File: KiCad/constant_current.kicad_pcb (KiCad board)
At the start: 2 copper layers, 15.2 x 16.5 mm, 18 parts, among them Q1 BC817-40

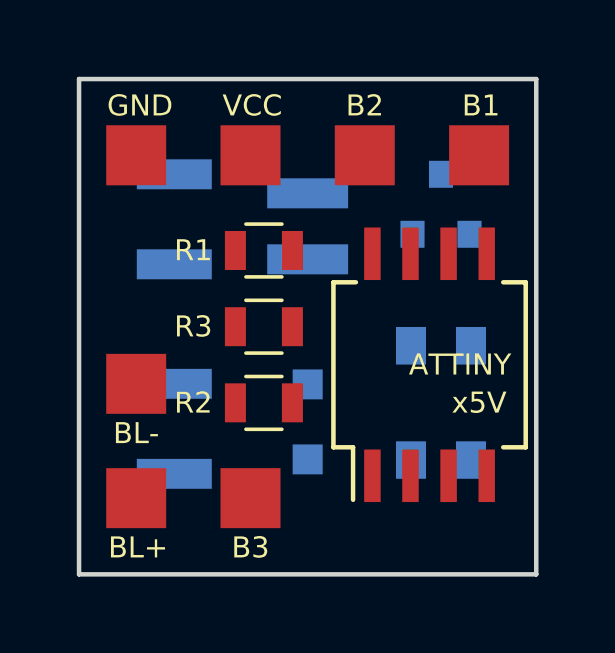
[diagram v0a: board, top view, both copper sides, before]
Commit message: Changed Footprint of Attiny
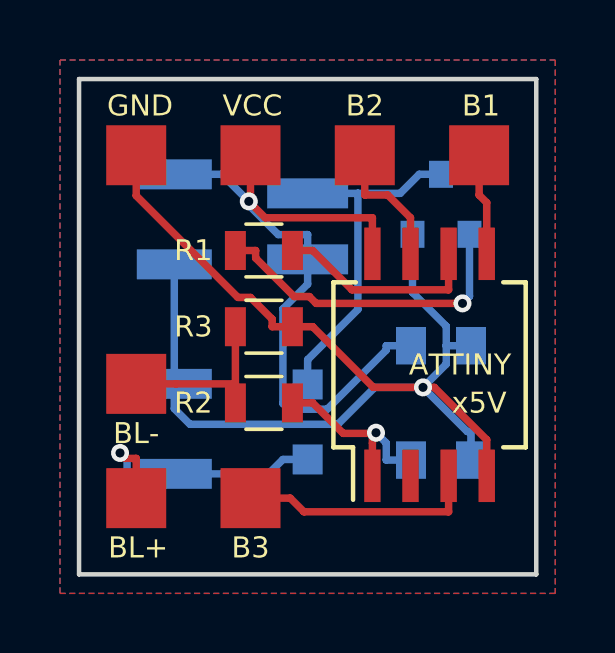
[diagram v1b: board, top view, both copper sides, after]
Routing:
- net GND: track 0.00 -> 41.5 mm, vias 0 -> 1
- net VCC: track 0.00 -> 23.7 mm, vias 0 -> 1
- net Net-(D1-Pad2): track 0.00 -> 11.8 mm
- net Net-(Q1-Pad1): track 0.00 -> 10.8 mm, vias 0 -> 1
- net Net-(C2-Pad1): track 0.00 -> 8.95 mm, vias 0 -> 1
- net Net-(IC1-Pad3): track 0.00 -> 7.99 mm
- net Net-(IC1-Pad6): track 0.00 -> 6.95 mm
- net Net-(C3-Pad2): track 0.00 -> 6.51 mm, vias 0 -> 1
- net Net-(R2-Pad2): track 0.00 -> 5.85 mm
- net Net-(IC1-Pad7): track 0.00 -> 4.36 mm
- net Net-(IC1-Pad5): track 0.00 -> 3.39 mm
- added copper zone on B.Cu, net GND
- added copper zone on F.Cu, net GND
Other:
- rule pad_to_mask_clearance: 0.2 -> 0

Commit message: changed inductor footprint
Changed inductor footprint for easyer handsoldering
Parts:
- L1: footprint 1212fps-inductor:1212fps-inductor -> 1212fps-inductor:1212fps-inductor-handsoldering
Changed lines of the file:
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@@
     (add_net VCC)
-  )
-  (module 1212fps-inductor:1212fps-inductor (layer B.Cu)
-    (at 116.84 61.425 270)
-    (descr "Inductor, 1212 FPS")
-    (tags "inductor ")
-    (attr smd)
-    (fp_text reference L1 (at 2.413 0.063 360) (layer B.SilkS)
-      (effects (font (size 0.7 0.7) (thickness 0.1)) (justify mirror))
-    )
-    (fp_text value 100µH (at 0 -3.5 270) (layer B.Fab) hide
-      (effects (font (size 1 1) (thickness 0.15)) (justify mirror))
-    )
-    (fp_line (start -1.778 1.524) (end -1.778 -1.524) (layer B.Fab) (width 0.15))
-    (fp_line (start -1.778 -1.524) (end 1.778 -1.524) (layer B.Fab) (width 0.15))
-    (fp_line (start 1.778 -1.524) (end 1.778 1.524) (layer B.Fab) (width 0.15))
-    (fp_line (start 1.778 1.524) (end -1.778 1.524) (layer B.Fab) (width 0.15))
-    (fp_line (start -1.905 1.6) (end 1.905 1.6) (layer B.SilkS) (width 0.15))
-    (fp_line (start -1.905 -1.6) (end 1.905 -1.6) (layer B.SilkS) (width 0.15))
-    (fp_line (start -2.159 1.778) (end -2.159 -1.778) (layer B.CrtYd) (width 0.05))
-    (fp_line (start -2.159 -1.778) (end 2.159 -1.778) (layer B.CrtYd) (width 0.05))
-    (fp_line (start 2.159 -1.778) (end 2.159 1.778) (layer B.CrtYd) (width 0.05))
-    (fp_line (start 2.159 1.778) (end -2.159 1.778) (layer B.CrtYd) (width 0.05))
-    (pad 1 smd rect (at -1.1 0 270) (size 1 2.7) (layers B.Cu B.Paste B.Mask)
-      (net 3 "Net-(D1-Pad2)"))
-    (pad 2 smd rect (at 1.1 0 270) (size 1 2.7) (layers B.Cu B.Paste B.Mask)
-      (net 2 VCC))
-    (model Inductors.3dshapes/Inductor_Taiyo-Yuden_MD-4040.wrl
-      (at (xyz 0 0 0))
-      (scale (xyz 1 1 1))
-      (rotate (xyz 0 0 0))
-    )
   )
   (module SMD_Packages:1Pin (layer F.Cu)
@@
       (at (xyz 0 0 0))
       (scale (xyz 1 1 1))
+      (rotate (xyz 0 0 0))
+    )
+  )
+  (module 1212fps-inductor:1212fps-inductor-handsoldering (layer B.Cu)
+    (at 116.84 61.425 270)
+    (descr "Inductor, 1212 FPS")
+    (tags "inductor ")
+    (attr smd)
+    (fp_text reference L1 (at 2.413 0.063 360) (layer B.SilkS)
+      (effects (font (size 0.7 0.7) (thickness 0.1)) (justify mirror))
+    )
+    (fp_text value 100µH (at 0 -3.5 270) (layer B.Fab) hide
+      (effects (font (size 1 1) (thickness 0.15)) (justify mirror))
+    )
+    (fp_line (start -1.778 1.524) (end -1.778 -1.524) (layer B.Fab) (width 0.15))
+    (fp_line (start -1.778 -1.524) (end 1.778 -1.524) (layer B.Fab) (width 0.15))
+    (fp_line (start 1.778 -1.524) (end 1.778 1.524) (layer B.Fab) (width 0.15))
+    (fp_line (start 1.778 1.524) (end -1.778 1.524) (layer B.Fab) (width 0.15))
+    (fp_line (start -1.905 1.6) (end 1.905 1.6) (layer B.SilkS) (width 0.15))
+    (fp_line (start -1.905 -1.6) (end 1.905 -1.6) (layer B.SilkS) (width 0.15))
+    (fp_line (start -2.159 1.778) (end -2.159 -1.778) (layer B.CrtYd) (width 0.05))
+    (fp_line (start -2.159 -1.778) (end 2.159 -1.778) (layer B.CrtYd) (width 0.05))
+    (fp_line (start 2.159 -1.778) (end 2.159 1.778) (layer B.CrtYd) (width 0.05))
+    (fp_line (start 2.159 1.778) (end -2.159 1.778) (layer B.CrtYd) (width 0.05))
+    (pad 1 smd rect (at -1.27 0 270) (size 1.3 2.7) (layers B.Cu B.Paste B.Mask)
+      (net 3 "Net-(D1-Pad2)"))
+    (pad 2 smd rect (at 1.27 0 270) (size 1.3 2.7) (layers B.Cu B.Paste B.Mask)
+      (net 2 VCC))
+    (model Inductors.3dshapes/Inductor_Taiyo-Yuden_MD-4040.wrl
+      (at (xyz 0 0 0))
+      (scale (xyz 1 1 1))
